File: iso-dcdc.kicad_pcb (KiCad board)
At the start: 2 copper layers, 10 parts, among them U1101 R05C05TE05S

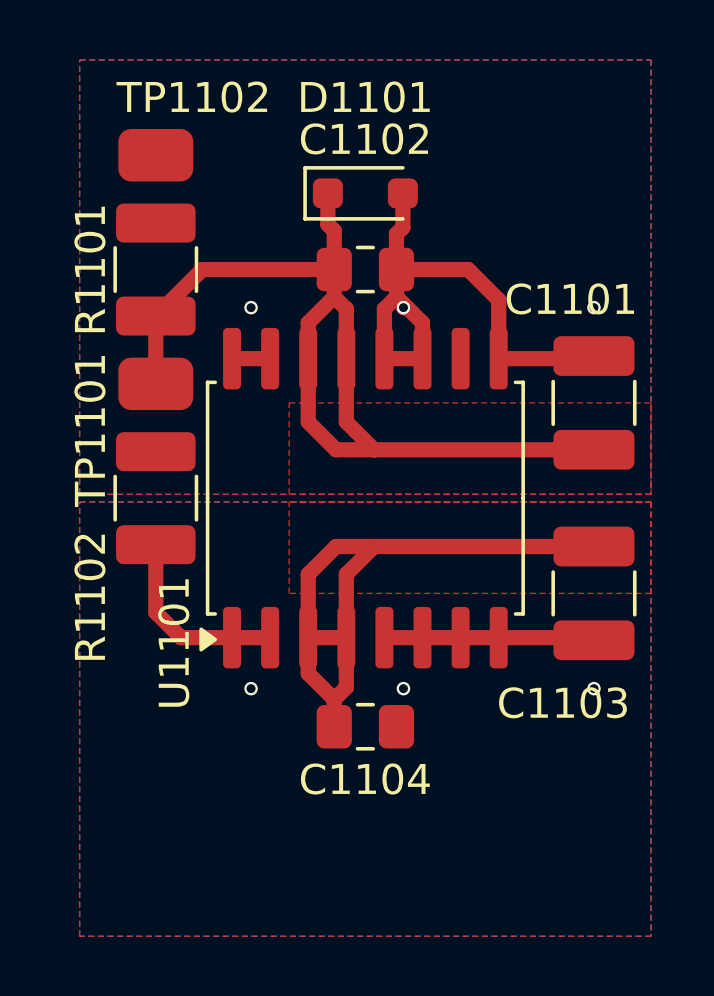
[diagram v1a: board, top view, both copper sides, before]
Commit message: edit silkscreen
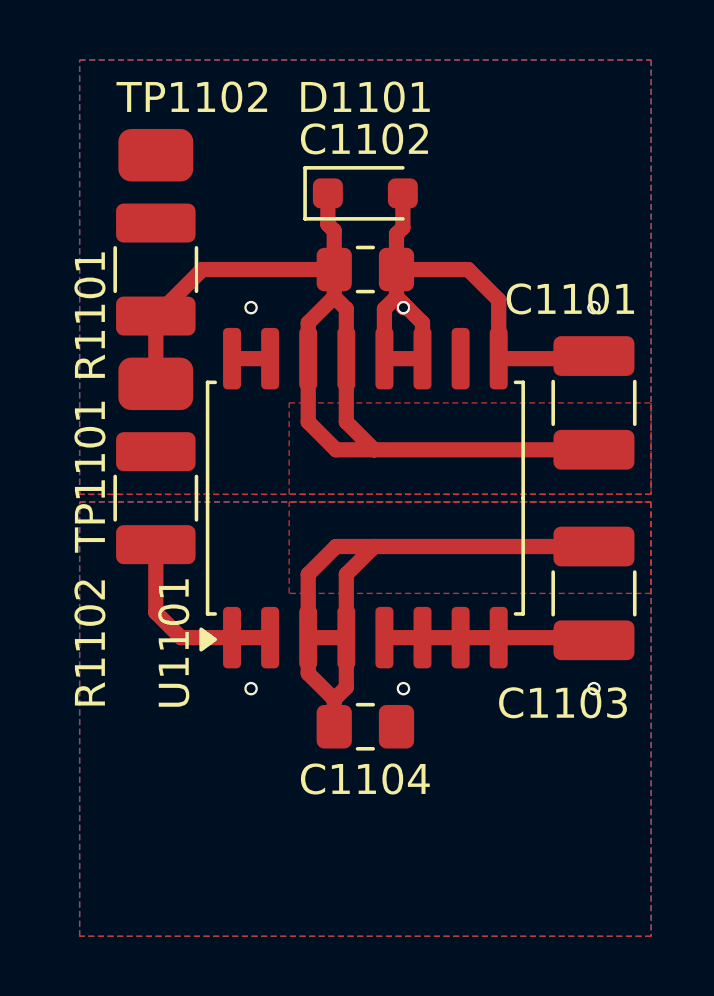
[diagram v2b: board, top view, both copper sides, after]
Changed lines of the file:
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@@
 		(tags "resistor handsolder")
 		(property "Reference" "R1102"
-			(at 3.302 2.159 90)
+			(at 4.826 2.159 90)
 			(layer "F.SilkS")
 			(effects
@@
 		(tags "resistor handsolder")
 		(property "Reference" "R1101"
-			(at 0 2.159 90)
+			(at 1.524 2.159 90)
 			(layer "F.SilkS")
 			(effects
@@
 		(tags "resistor")
 		(property "Reference" "TP1101"
-			(at -2.159 1.524 90)
-			(layer "F.SilkS")
-			(effects
+			(at -2.159 3.048 90)
+			(layer "F.SilkS")
+			(effects
